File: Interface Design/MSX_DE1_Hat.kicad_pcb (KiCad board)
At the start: 2 copper layers, 103 x 66 mm, 31 parts, among them J1 DE1 GPIO, J2 Conn_01x03_Male, J3 Conn_01x03_Male, J4 Conn_01x03_Male, J5 Conn_01x03_Male, J6 Conn_01x03_Male, J7 Conn_01x03_Male, U1 74LVC245A, U2 74LVC245A, U3 74LVC245A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

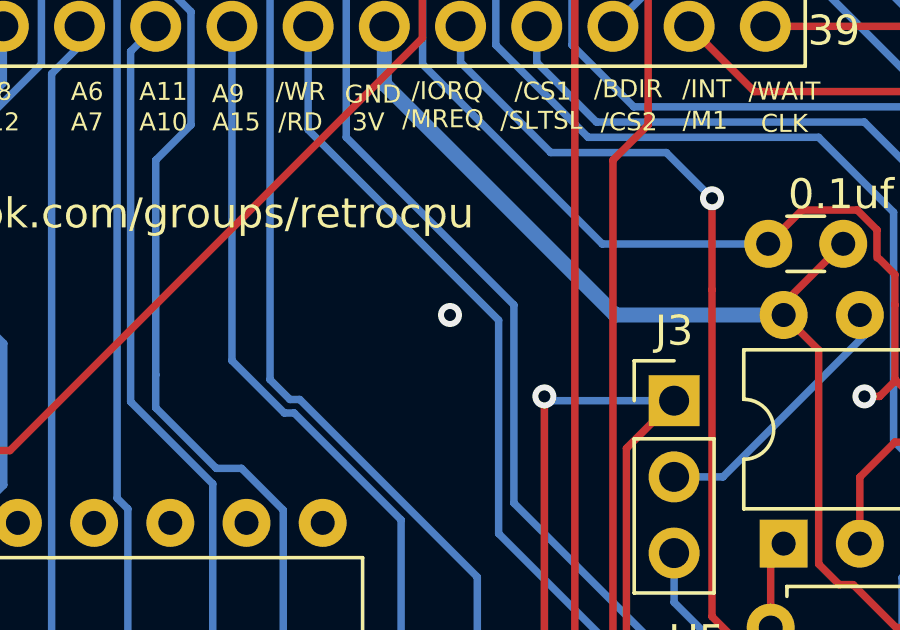
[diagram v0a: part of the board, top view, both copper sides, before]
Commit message: Renamed the project from MSX IDC Interface to MSX DE1 hat
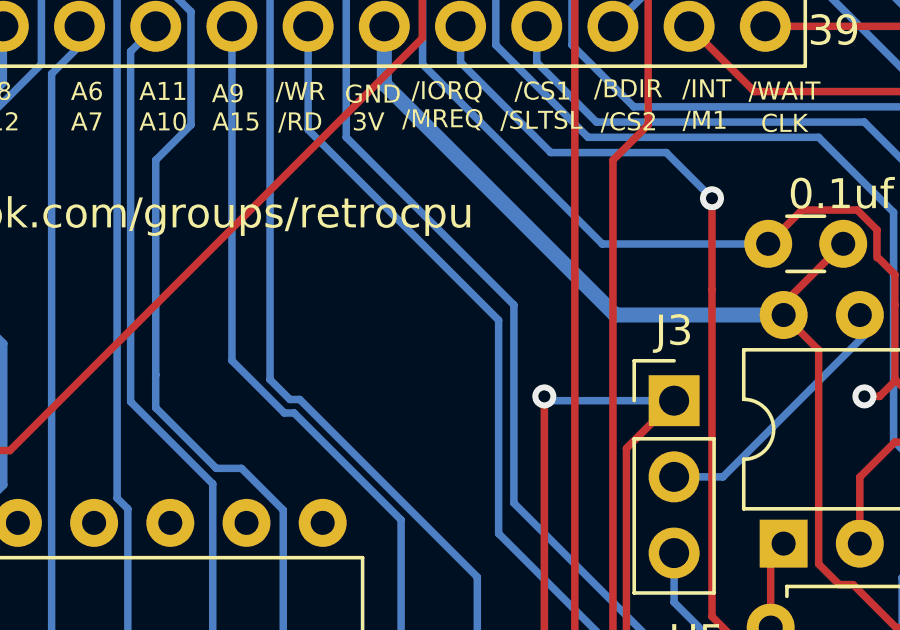
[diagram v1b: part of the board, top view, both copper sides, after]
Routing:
- net (no net): vias 1 -> 0
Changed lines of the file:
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@@
     (descr "C, Disc series, Radial, pin pitch=2.50mm, , diameter*width=3.0*1.6mm^2, Capacitor, http://www.vishay.com/docs/45233/krseries.pdf")
     (tags "C Disc series Radial pin pitch 2.50mm  diameter 3.0mm width 1.6mm Capacitor")
-    (property "Sheetfile" "MSX_IDC_Interface.kicad_sch")
+    (property "Sheetfile" "MSX_DE1_Hat.kicad_sch")
     (property "Sheetname" "")
     (attr through_hole)
@@
     (descr "C, Disc series, Radial, pin pitch=2.50mm, , diameter*width=3.0*1.6mm^2, Capacitor, http://www.vishay.com/docs/45233/krseries.pdf")
     (tags "C Disc series Radial pin pitch 2.50mm  diameter 3.0mm width 1.6mm Capacitor")
-    (property "Sheetfile" "MSX_IDC_Interface.kicad_sch")
+    (property "Sheetfile" "MSX_DE1_Hat.kicad_sch")
     (property "Sheetname" "")
     (attr through_hole)
@@
     (descr "C, Disc series, Radial, pin pitch=2.50mm, , diameter*width=3.0*1.6mm^2, Capacitor, http://www.vishay.com/docs/45233/krseries.pdf")
     (tags "C Disc series Radial pin pitch 2.50mm  diameter 3.0mm width 1.6mm Capacitor")
-    (property "Sheetfile" "MSX_IDC_Interface.kicad_sch")
+    (property "Sheetfile" "MSX_DE1_Hat.kicad_sch")
     (property "Sheetname" "")
     (attr through_hole)
@@
     (descr "Through hole straight pin header, 1x03, 2.54mm pitch, single row")
     (tags "Through hole pin header THT 1x03 2.54mm single row")
-    (property "Sheetfile" "MSX_IDC_Interface.kicad_sch")
+    (property "Sheetfile" "MSX_DE1_Hat.kicad_sch")
     (property "Sheetname" "")
     (attr through_hole)
@@
     (descr "Through hole straight pin header, 2x20, 2.54mm pitch, double rows")
     (tags "Through hole pin header THT 2x20 2.54mm double row")
-    (property "Sheetfile" "MSX_IDC_Interface.kicad_sch")
+    (property "Sheetfile" "MSX_DE1_Hat.kicad_sch")
     (property "Sheetname" "")
     (attr through_hole)
@@
     (descr "C, Disc series, Radial, pin pitch=2.50mm, , diameter*width=3.0*1.6mm^2, Capacitor, http://www.vishay.com/docs/45233/krseries.pdf")
     (tags "C Disc series Radial pin pitch 2.50mm  diameter 3.0mm width 1.6mm Capacitor")
-    (property "Sheetfile" "MSX_IDC_Interface.kicad_sch")
+    (property "Sheetfile" "MSX_DE1_Hat.kicad_sch")
     (property "Sheetname" "")
     (attr through_hole)
@@
     (descr "20-lead though-hole mounted DIP package, row spacing 7.62 mm (300 mils)")
     (tags "THT DIP DIL PDIP 2.54mm 7.62mm 300mil")
-    (property "Sheetfile" "MSX_IDC_Interface.kicad_sch")
+    (property "Sheetfile" "MSX_DE1_Hat.kicad_sch")
     (property "Sheetname" "")
     (attr through_hole)
@@
     (descr "C, Disc series, Radial, pin pitch=2.50mm, , diameter*width=3.0*1.6mm^2, Capacitor, http://www.vishay.com/docs/45233/krseries.pdf")
     (tags "C Disc series Radial pin pitch 2.50mm  diameter 3.0mm width 1.6mm Capacitor")
-    (property "Sheetfile" "MSX_IDC_Interface.kicad_sch")
+    (property "Sheetfile" "MSX_DE1_Hat.kicad_sch")
     (property "Sheetname" "")
     (attr through_hole)
@@
     (descr "Resistor, Axial_DIN0207 series, Axial, Horizontal, pin pitch=7.62mm, 0.25W = 1/4W, length*diameter=6.3*2.5mm^2, http://cdn-reichelt.de/documents/datenblatt/B400/1_4W%23YAG.pdf")
     (tags "Resistor Axial_DIN0207 series Axial Horizontal pin pitch 7.62mm 0.25W = 1/4W length 6.3mm diameter 2.5mm")
-    (property "Sheetfile" "MSX_IDC_Interface.kicad_sch")
+    (property "Sheetfile" "MSX_DE1_Hat.kicad_sch")
     (property "Sheetname" "")
     (attr through_hole)
@@
     (descr "Through hole straight pin header, 1x03, 2.54mm pitch, single row")
     (tags "Through hole pin header THT 1x03 2.54mm single row")
-    (property "Sheetfile" "MSX_IDC_Interface.kicad_sch")
+    (property "Sheetfile" "MSX_DE1_Hat.kicad_sch")
     (property "Sheetname" "")
     (attr through_hole)
@@
     (descr "20-lead though-hole mounted DIP package, row spacing 7.62 mm (300 mils)")
     (tags "THT DIP DIL PDIP 2.54mm 7.62mm 300mil")
-    (property "Sheetfile" "MSX_IDC_Interface.kicad_sch")
+    (property "Sheetfile" "MSX_DE1_Hat.kicad_sch")
     (property "Sheetname" "")
     (attr through_hole)
@@
   (footprint "Roni Footprints:MSX_CART" (layer "F.Cu")
     (at 101.6 50.8)
-    (property "Sheetfile" "MSX_IDC_Interface.kicad_sch")
+    (property "Sheetfile" "MSX_DE1_Hat.kicad_sch")
     (property "Sheetname" "")
     (attr through_hole)
@@
     (descr "Through hole straight pin header, 1x03, 2.54mm pitch, single row")
     (tags "Through hole pin header THT 1x03 2.54mm single row")
-    (property "Sheetfile" "MSX_IDC_Interface.kicad_sch")
+    (property "Sheetfile" "MSX_DE1_Hat.kicad_sch")
     (property "Sheetname" "")
     (attr through_hole)
@@
     (descr "Through hole straight pin header, 1x03, 2.54mm pitch, single row")
     (tags "Through hole pin header THT 1x03 2.54mm single row")
-    (property "Sheetfile" "MSX_IDC_Interface.kicad_sch")
+    (property "Sheetfile" "MSX_DE1_Hat.kicad_sch")
     (property "Sheetname" "")
     (attr through_hole)
@@
     (descr "Through hole straight pin header, 1x03, 2.54mm pitch, single row")
     (tags "Through hole pin header THT 1x03 2.54mm single row")
-    (property "Sheetfile" "MSX_IDC_Interface.kicad_sch")
+    (property "Sheetfile" "MSX_DE1_Hat.kicad_sch")
     (property "Sheetname" "")
     (attr through_hole)
@@
     (descr "Resistor, Axial_DIN0207 series, Axial, Horizontal, pin pitch=7.62mm, 0.25W = 1/4W, length*diameter=6.3*2.5mm^2, http://cdn-reichelt.de/documents/datenblatt/B400/1_4W%23YAG.pdf")
     (tags "Resistor Axial_DIN0207 series Axial Horizontal pin pitch 7.62mm 0.25W = 1/4W length 6.3mm diameter 2.5mm")
-    (property "Sheetfile" "MSX_IDC_Interface.kicad_sch")
+    (property "Sheetfile" "MSX_DE1_Hat.kicad_sch")
     (property "Sheetname" "")
     (attr through_hole)
@@
     (descr "Resistor, Axial_DIN0207 series, Axial, Horizontal, pin pitch=7.62mm, 0.25W = 1/4W, length*diameter=6.3*2.5mm^2, http://cdn-reichelt.de/documents/datenblatt/B400/1_4W%23YAG.pdf")
     (tags "Resistor Axial_DIN0207 series Axial Horizontal pin pitch 7.62mm 0.25W = 1/4W length 6.3mm diameter 2.5mm")
-    (property "Sheetfile" "MSX_IDC_Interface.kicad_sch")
+    (property "Sheetfile" "MSX_DE1_Hat.kicad_sch")
     (property "Sheetname" "")
     (attr through_hole)
@@
     (descr "14-lead though-hole mounted DIP package, row spacing 7.62 mm (300 mils)")
     (tags "THT DIP DIL PDIP 2.54mm 7.62mm 300mil")
-    (property "Sheetfile" "MSX_IDC_Interface.kicad_sch")
+    (property "Sheetfile" "MSX_DE1_Hat.kicad_sch")
     (property "Sheetname" "")
     (attr through_hole)
@@
     (descr "Resistor, Axial_DIN0207 series, Axial, Horizontal, pin pitch=7.62mm, 0.25W = 1/4W, length*diameter=6.3*2.5mm^2, http://cdn-reichelt.de/documents/datenblatt/B400/1_4W%23YAG.pdf")
     (tags "Resistor Axial_DIN0207 series Axial Horizontal pin pitch 7.62mm 0.25W = 1/4W length 6.3mm diameter 2.5mm")
-    (property "Sheetfile" "MSX_IDC_Interface.kicad_sch")
+    (property "Sheetfile" "MSX_DE1_Hat.kicad_sch")
     (property "Sheetname" "")
     (attr through_hole)
@@
     (descr "20-lead though-hole mounted DIP package, row spacing 7.62 mm (300 mils)")
     (tags "THT DIP DIL PDIP 2.54mm 7.62mm 300mil")
-    (property "Sheetfile" "MSX_IDC_Interface.kicad_sch")
+    (property "Sheetfile" "MSX_DE1_Hat.kicad_sch")
     (property "Sheetname" "")
     (attr through_hole)
@@
     (descr "20-lead though-hole mounted DIP package, row spacing 7.62 mm (300 mils)")
     (tags "THT DIP DIL PDIP 2.54mm 7.62mm 300mil")
-    (property "Sheetfile" "MSX_IDC_Interface.kicad_sch")
+    (property "Sheetfile" "MSX_DE1_Hat.kicad_sch")
     (property "Sheetname" "")
     (attr through_hole)
@@
     (descr "Resistor, Axial_DIN0207 series, Axial, Horizontal, pin pitch=7.62mm, 0.25W = 1/4W, length*diameter=6.3*2.5mm^2, http://cdn-reichelt.de/documents/datenblatt/B400/1_4W%23YAG.pdf")
     (tags "Resistor Axial_DIN0207 series Axial Horizontal pin pitch 7.62mm 0.25W = 1/4W length 6.3mm diameter 2.5mm")
-    (property "Sheetfile" "MSX_IDC_Interface.kicad_sch")
+    (property "Sheetfile" "MSX_DE1_Hat.kicad_sch")
     (property "Sheetname" "")
     (attr through_hole)
@@
     (descr "C, Disc series, Radial, pin pitch=2.50mm, , diameter*width=3.0*1.6mm^2, Capacitor, http://www.vishay.com/docs/45233/krseries.pdf")
     (tags "C Disc series Radial pin pitch 2.50mm  diameter 3.0mm width 1.6mm Capacitor")
-    (property "Sheetfile" "MSX_IDC_Interface.kicad_sch")
+    (property "Sheetfile" "MSX_DE1_Hat.kicad_sch")
     (property "Sheetname" "")
     (attr through_hole)
@@
     (descr "Through hole straight pin header, 1x03, 2.54mm pitch, single row")
     (tags "Through hole pin header THT 1x03 2.54mm single row")
-    (property "Sheetfile" "MSX_IDC_Interface.kicad_sch")
+    (property "Sheetfile" "MSX_DE1_Hat.kicad_sch")
     (property "Sheetname" "")
     (attr through_hole)
@@
     (descr "20-lead though-hole mounted DIP package, row spacing 7.62 mm (300 mils)")
     (tags "THT DIP DIL PDIP 2.54mm 7.62mm 300mil")
-    (property "Sheetfile" "MSX_IDC_Interface.kicad_sch")
+    (property "Sheetfile" "MSX_DE1_Hat.kicad_sch")
     (property "Sheetname" "")
     (attr through_hole)
@@
     (effects (font (size 0.6 0.6) (thickness 0.11)))
   )
-  (via (at 115.21852 34.370766) (size 0.8) (drill 0.4) (layers "F.Cu" "B.Cu") (free) (net 0))
   (segment (start 129.032 37.084) (end 129.54 37.084) (width 0.25) (layer "F.Cu") (net 1))
   (segment (start 87.376 64.516) (end 90.162925 61.729075) (width 0.25) (layer "F.Cu") (net 1))
